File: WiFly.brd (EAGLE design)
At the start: 45.7 x 35.9 mm, 33 parts

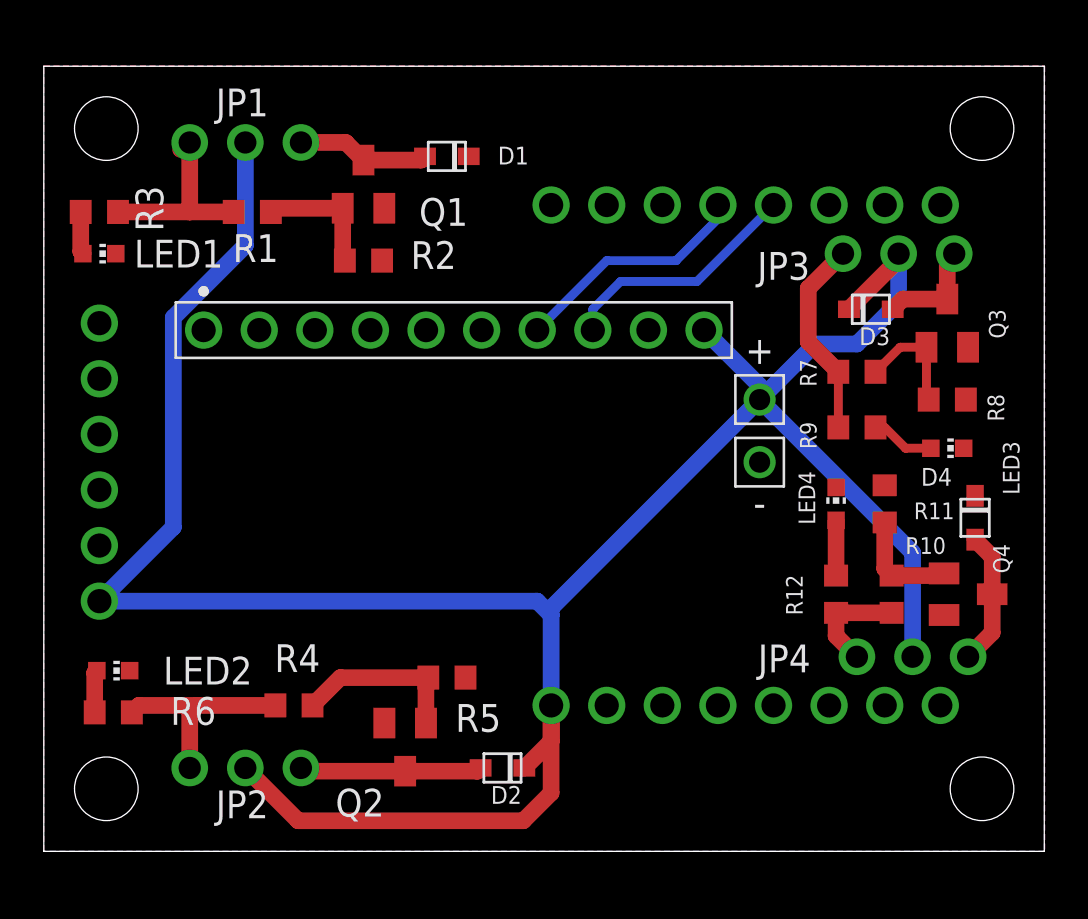
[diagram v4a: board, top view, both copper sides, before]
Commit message: Routed remaining wires and polygon pour, no errors ERC detected
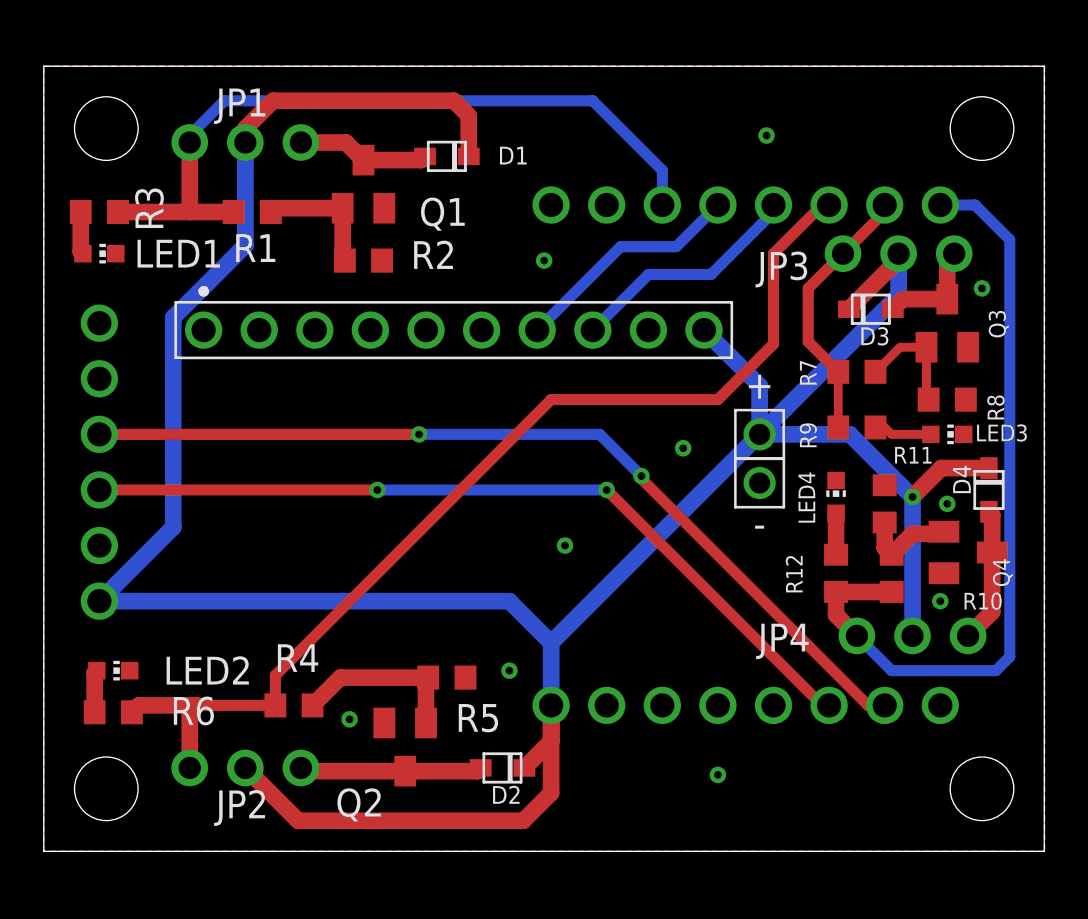
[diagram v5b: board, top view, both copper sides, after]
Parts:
- moved Q4 1.91 mm to (41.6, 11.7)
- moved + 1.59 mm to (32.1, 17.1)
- moved D4 1.42 mm to (42.5, 14.6)
- moved - 0.95 mm to (32.1, 14.9)
- moved R10 0.95 mm to (38.1, 10.8)
- moved R12 0.95 mm to (35.6, 10.8)
- moved JP4 0.95 mm to (39.1, 7.94)
- moved LED3 0.63 mm to (40.6, 17.1)
- moved LED4 0.32 mm to (35.6, 14.3)
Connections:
- removed net TODO1: JP4.1, R10.1, R12.2
- removed net TODO2: JP3.1, R7.1, R9.2
- removed net TODO3: JP2.1, R4.1, R6.2
- removed net TODO4: JP1.1, R1.1, R3.2
- net GPIO12: now also JP1.1, R1.1, R3.2
- net GPIO14: now also JP2.1, R4.1, R6.2
- net GPIO2: now also JP3.1, R7.1, R9.2
- net GPIO4: now also JP4.1, R10.1, R12.2
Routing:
- net GPIO14: track 0.00 -> 47.7 mm
- net TX: track 0.00 -> 41.1 mm, vias 0 -> 2
- net RX: track 0.00 -> 37.4 mm, vias 0 -> 2
- net GPIO4: track 0.00 -> 35.7 mm
- net GPIO12: track 0.00 -> 33.9 mm
- net VCC: track 118.2 -> 136.6 mm, vias 0 -> 1
- net GPIO2: track 0.00 -> 12.2 mm
- net TODO3: track 9.68 -> 0.00 mm
- net TODO2: track 9.16 -> 0.00 mm
- net TODO4: track 9.01 -> 0.00 mm
- net TODO1: track 4.94 -> 0.00 mm
- net N$15: track 2.53 -> 1.89 mm
- net N$14: track 4.99 -> 4.43 mm

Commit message: Widened board a bit to provide clearance for mounting screws. Rev 1 FingersCrossed
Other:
- board size 45.7 x 35.9 mm -> 45.7 x 37.5 mm
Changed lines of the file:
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@@
 <board>
 <plain>
-<wire x1="-0.635" y1="-1.905" x2="45.0725" y2="-1.905" width="0" layer="20"/>
-<wire x1="45.0725" y1="-1.905" x2="45.0725" y2="33.9625" width="0" layer="20"/>
-<wire x1="45.0725" y1="33.9625" x2="-0.635" y2="33.9625" width="0" layer="20"/>
-<wire x1="-0.635" y1="33.9625" x2="-0.635" y2="-1.905" width="0" layer="20"/>
-<hole x="2.2225" y="31.115" drill="2.905759375"/>
-<hole x="42.2275" y="31.115" drill="2.905759375"/>
-<hole x="2.2225" y="0.9525" drill="2.905759375"/>
-<hole x="42.2275" y="0.9525" drill="2.905759375"/>
+<wire x1="-0.635" y1="-2.8575" x2="45.0725" y2="-2.8575" width="0" layer="20"/>
+<wire x1="45.0725" y1="-2.8575" x2="45.0725" y2="34.5975" width="0" layer="20"/>
+<wire x1="45.0725" y1="34.5975" x2="-0.635" y2="34.5975" width="0" layer="20"/>
+<wire x1="-0.635" y1="34.5975" x2="-0.635" y2="-2.8575" width="0" layer="20"/>
+<hole x="2.2225" y="31.75" drill="2.905759375"/>
+<hole x="42.2275" y="31.75" drill="2.905759375"/>
+<hole x="2.2225" y="0" drill="2.905759375"/>
+<hole x="42.2275" y="0" drill="2.905759375"/>
 </plain>
 <attributes>
@@
 <contactref element="-" pad="1"/>
 <polygon width="0.4064" layer="16" isolate="0.254">
-<vertex x="-0.635" y="-1.905"/>
-<vertex x="-0.635" y="33.9725"/>
-<vertex x="45.085" y="33.9725"/>
-<vertex x="45.085" y="-1.905"/>
+<vertex x="-0.635" y="-2.8575"/>
+<vertex x="-0.635" y="34.6075"/>
+<vertex x="45.085" y="34.6075"/>
+<vertex x="45.085" y="-2.8575"/>
 </polygon>
 <polygon width="0.4064" layer="1" isolate="0.254">
-<vertex x="-0.635" y="-1.905"/>
-<vertex x="-0.635" y="33.9725"/>
-<vertex x="45.085" y="33.9725"/>
-<vertex x="45.085" y="-1.905"/>
+<vertex x="-0.635" y="-2.8575"/>
+<vertex x="-0.635" y="34.6075"/>
+<vertex x="45.085" y="34.6075"/>
+<vertex x="45.085" y="-2.8575"/>
 </polygon>
 <contactref element="U$2" pad="12"/>
@@
 <via x="40.64" y="13.97" extent="1-16" drill="0.35"/>
 <via x="42.2275" y="23.8125" extent="1-16" drill="0.35"/>
+<via x="10.4775" y="19.3675" extent="1-16" drill="0.35"/>
+<via x="8.5725" y="12.065" extent="1-16" drill="0.35"/>
+<via x="31.75" y="12.065" extent="1-16" drill="0.35"/>
 </signal>
 <signal name="N$2">
@@
 <contactref element="U$2" pad="14"/>
 <contactref element="U$3" pad="3"/>
-<wire x1="1.905" y1="14.605" x2="14.605" y2="14.605" width="0.508" layer="1"/>
-<via x="14.605" y="14.605" extent="1-16" drill="0.35"/>
-<wire x1="14.605" y1="14.605" x2="25.0825" y2="14.605" width="0.508" layer="16"/>
+<wire x1="1.905" y1="14.605" x2="13.335" y2="14.605" width="0.508" layer="1"/>
+<via x="13.335" y="14.605" extent="1-16" drill="0.35"/>
+<wire x1="13.335" y1="14.605" x2="25.0825" y2="14.605" width="0.508" layer="16"/>
 <via x="25.0825" y="14.605" extent="1-16" drill="0.35"/>
 <wire x1="34.925" y1="4.7625" x2="25.0825" y2="14.605" width="0.508" layer="1"/>
@@
 <contactref element="U$2" pad="15"/>
 <contactref element="U$3" pad="4"/>
-<via x="16.51" y="17.145" extent="1-16" drill="0.35"/>
-<wire x1="16.51" y1="17.145" x2="24.765" y2="17.145" width="0.508" layer="16"/>
+<via x="14.9225" y="17.145" extent="1-16" drill="0.35"/>
+<wire x1="14.9225" y1="17.145" x2="24.765" y2="17.145" width="0.508" layer="16"/>
 <wire x1="24.765" y1="17.145" x2="26.67" y2="15.24" width="0.508" layer="16"/>
 <via x="26.67" y="15.24" extent="1-16" drill="0.35"/>
@@
 <wire x1="26.67" y1="15.24" x2="26.67" y2="15.115425" width="0.508" layer="1"/>
 <wire x1="37.022925" y1="4.7625" x2="37.7825" y2="4.7625" width="0.508" layer="1"/>
-<wire x1="1.905" y1="17.145" x2="16.51" y2="17.145" width="0.508" layer="1"/>
+<wire x1="1.905" y1="17.145" x2="14.9225" y2="17.145" width="0.508" layer="1"/>
 </signal>
 <signal name="GPIO14">

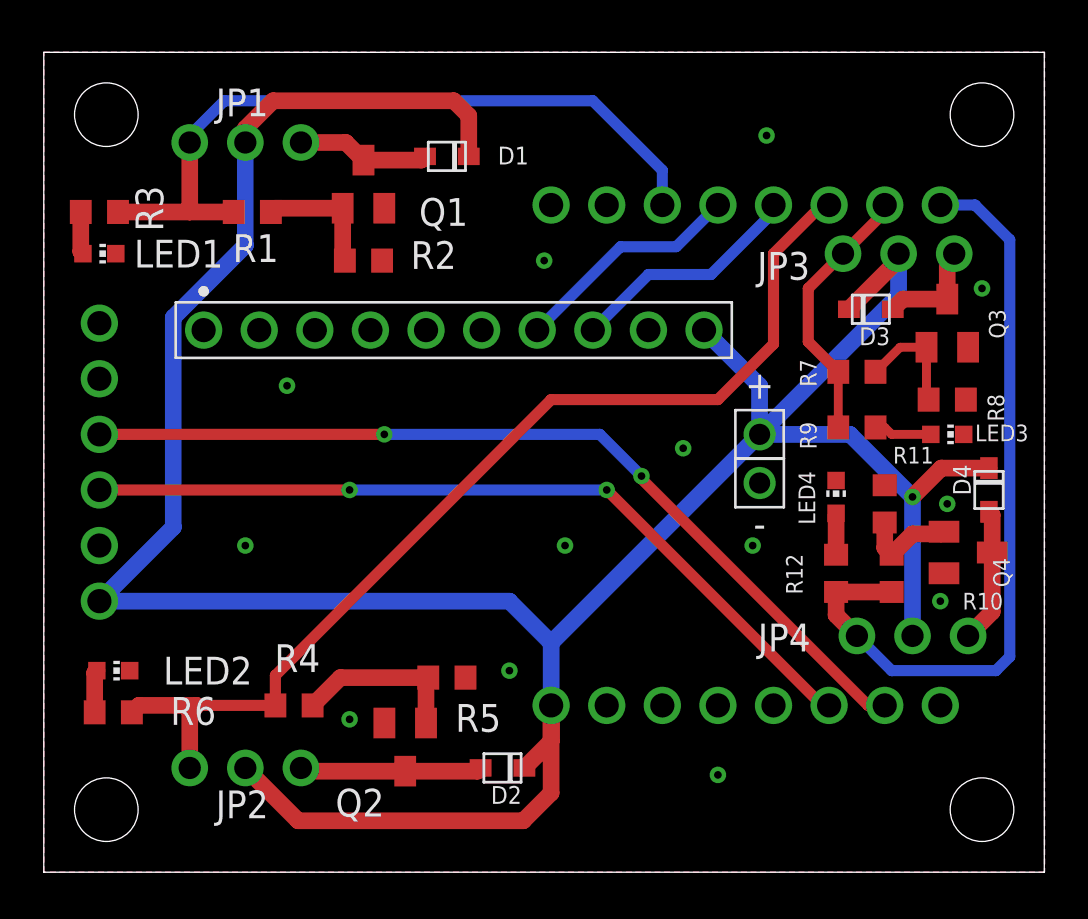
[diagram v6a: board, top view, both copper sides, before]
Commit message: Fix ESP32 layout and slide location down
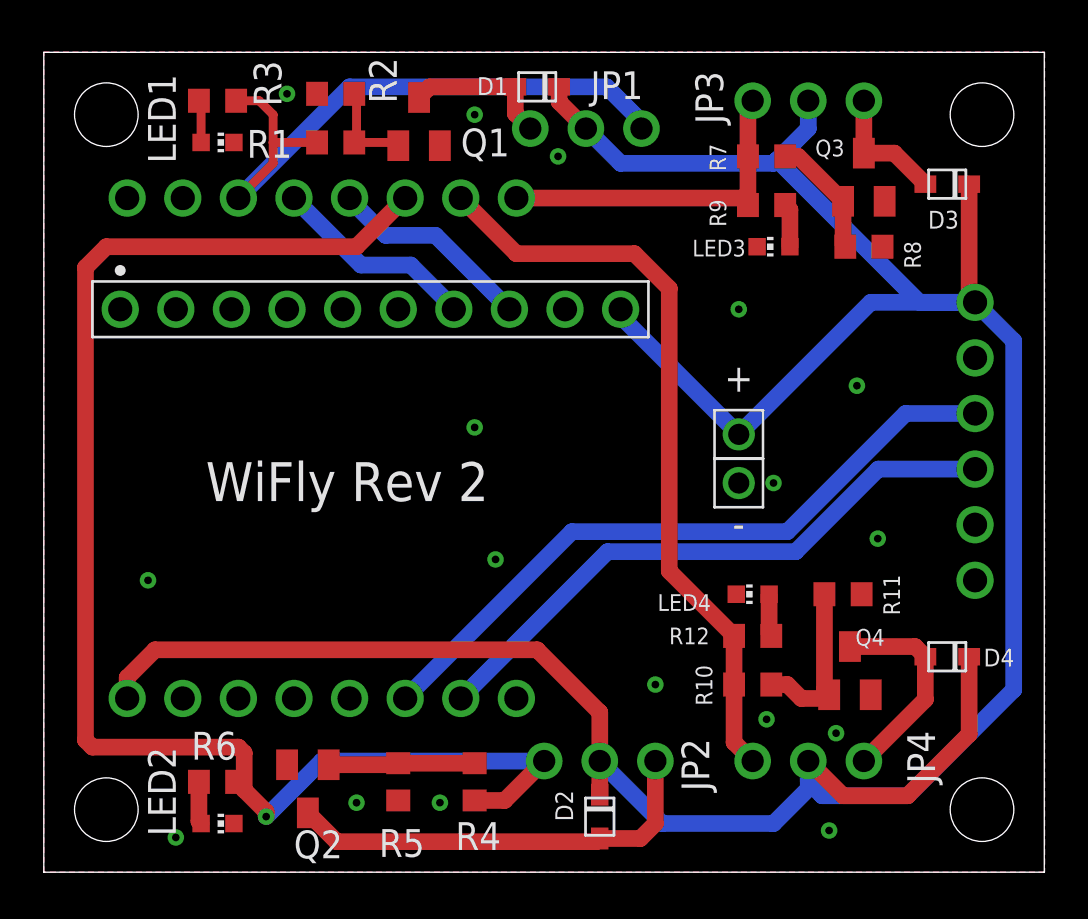
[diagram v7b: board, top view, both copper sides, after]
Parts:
- moved U$3 42.3 mm to (41.9, 23.2), turned to 270 degrees
- moved U$2 19.4 mm to (21.0, 27.9)
- moved JP2 16.2 mm to (24.8, 2.22)
- moved JP1 15.6 mm to (24.1, 31.1), turned to 180 degrees
- moved LED3 11.7 mm to (32.7, 25.7), turned to 90 degrees
- moved R9 11.0 mm to (32.4, 27.6)
- moved R7 10.7 mm to (32.4, 29.8)
- moved R4 8.96 mm to (19.1, 1.27), turned to 90 degrees
- moved LED2 8.45 mm to (7.30, -0.64)
- moved R10 8.13 mm to (31.8, 5.71), turned to 0 degrees
- moved JP3 8.11 mm to (34.3, 32.4)
- moved R8 7.96 mm to (36.8, 25.7)
- moved D4 7.85 mm to (40.6, 6.99), turned to 0 degrees
- moved R2 7.73 mm to (12.7, 32.7), turned to 0 degrees
- moved Q3 7.68 mm to (36.8, 28.9)
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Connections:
- net GPIO2: now also JP4.1, R10.1, R12.2; no longer JP3.1, R7.1, R9.2
- net GPIO4: now also JP3.1, R7.1, R9.2; no longer JP4.1, R10.1, R12.2
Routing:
- net GPIO2: track 12.2 -> 34.4 mm
- net GPIO4: track 35.7 -> 15.6 mm
- net GPIO14: track 47.7 -> 66.5 mm, vias 0 -> 1
- net TX: track 41.1 -> 27.8 mm, vias 2 -> 0
- net N$8: track 8.33 -> 19.6 mm
- net RX: track 37.4 -> 31.4 mm, vias 2 -> 0
- net GPIO12: track 33.9 -> 29.9 mm
- net N$16: track 6.18 -> 9.56 mm
- net N$14: track 4.43 -> 7.66 mm
- net VCC: track 136.6 -> 138.1 mm, vias 1 -> 0
- net N$2: track 5.78 -> 4.34 mm
- net SCL: track 10.8 -> 9.44 mm
- net N$6: track 7.93 -> 6.70 mm
- net SDA: track 10.6 -> 9.44 mm
- net N$12: track 4.89 -> 5.79 mm
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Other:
- board text added: "WiFly Rev 2"

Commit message: Make compatible with lower power battery connection
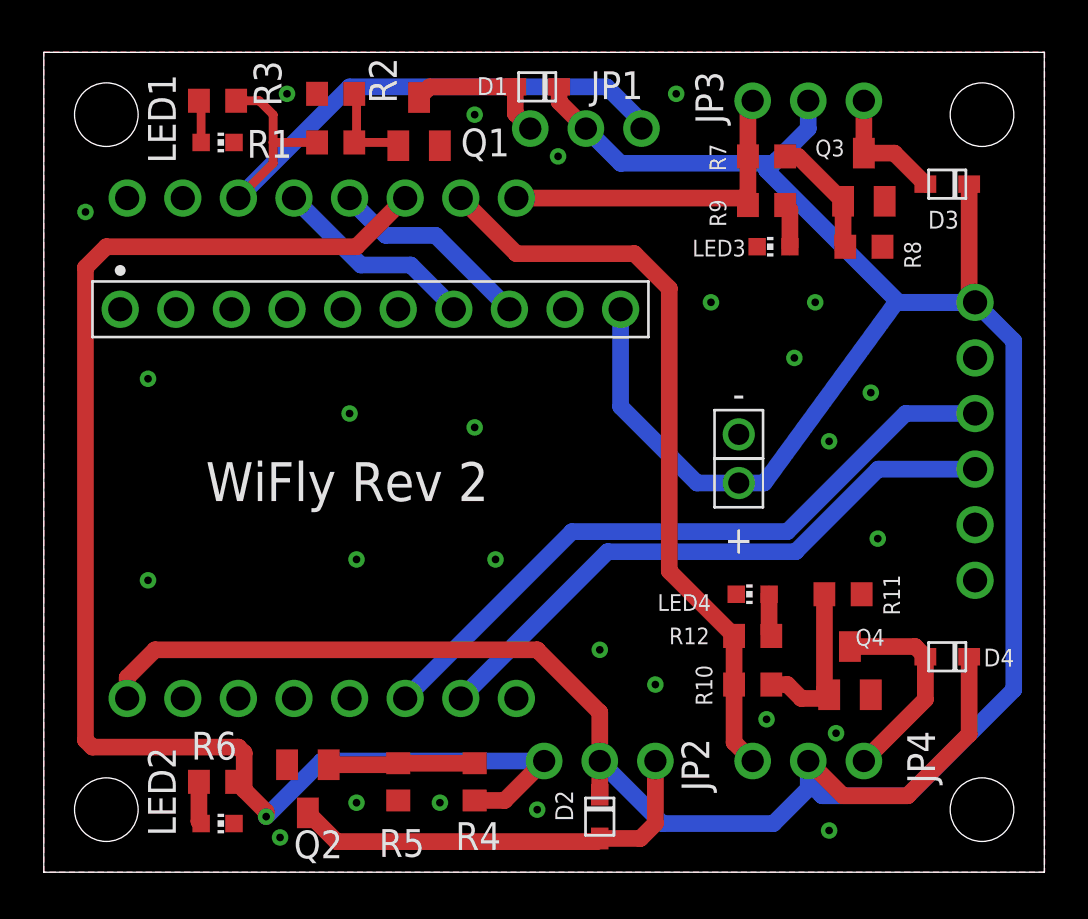
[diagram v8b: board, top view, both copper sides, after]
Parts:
- moved + 2.22 mm to (31.1, 14.9), turned to 270 degrees
- moved - 2.22 mm to (31.1, 17.1), turned to 0 degrees
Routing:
- net VCC: track 138.1 -> 143.8 mm
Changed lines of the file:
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@@
 <attribute name="VALUE" x="32.639" y="9.9695" size="1.27" layer="27" rot="R180"/>
 </element>
-<element name="+" library="WiFlyParts" package="HDRV1W64P0_1X1_193X193X447B" package3d_urn="urn:adsk.eagle:package:26906388/1" value="22AWG22AWG-MALE" x="31.115" y="17.145" smashed="yes" rot="R90">
-<attribute name="NAME" x="31.115" y="20.3644" size="1.27" layer="25" rot="R180" align="bottom-center"/>
+<element name="+" library="WiFlyParts" package="HDRV1W64P0_1X1_193X193X447B" package3d_urn="urn:adsk.eagle:package:26906388/1" value="22AWG22AWG-MALE" x="31.115" y="14.9225" smashed="yes" rot="R270">
+<attribute name="NAME" x="31.115" y="11.7031" size="1.27" layer="25" align="bottom-center"/>
 </element>
-<element name="-" library="WiFlyParts" package="HDRV1W64P0_1X1_193X193X447B" package3d_urn="urn:adsk.eagle:package:26906388/1" value="22AWG22AWG-MALE" x="31.115" y="14.9225" smashed="yes" rot="R180">
-<attribute name="NAME" x="31.115" y="13.6969" size="1.27" layer="25" rot="R180" align="bottom-center"/>
+<element name="-" library="WiFlyParts" package="HDRV1W64P0_1X1_193X193X447B" package3d_urn="urn:adsk.eagle:package:26906388/1" value="22AWG22AWG-MALE" x="31.115" y="17.145" smashed="yes">
+<attribute name="NAME" x="31.115" y="18.3706" size="1.27" layer="25" align="bottom-center"/>
 </element>
 </elements>
@@
 <via x="32.385" y="4.1275" extent="1-16" drill="0.35"/>
 <via x="35.56" y="3.4925" extent="1-16" drill="0.35"/>
-<via x="5.3975" y="-1.27" extent="1-16" drill="0.35"/>
+<via x="10.16" y="-1.27" extent="1-16" drill="0.35"/>
 <via x="10.4775" y="32.7025" extent="1-16" drill="0.35"/>
 <via x="13.6525" y="0.3175" extent="1-16" drill="0.35"/>
@@
 <via x="19.05" y="31.75" extent="1-16" drill="0.35"/>
 <via x="35.2425" y="-0.9525" extent="1-16" drill="0.35"/>
-<via x="36.5125" y="19.3675" extent="1-16" drill="0.35"/>
+<via x="37.1475" y="19.05" extent="1-16" drill="0.35"/>
 <via x="19.05" y="17.4625" extent="1-16" drill="0.35"/>
 <via x="37.465" y="12.3825" extent="1-16" drill="0.35"/>
 <via x="4.1275" y="10.4775" extent="1-16" drill="0.35"/>
 <via x="27.305" y="5.715" extent="1-16" drill="0.35"/>
-<via x="31.115" y="22.86" extent="1-16" drill="0.35"/>
+<via x="29.845" y="23.1775" extent="1-16" drill="0.35"/>
 <via x="22.86" y="29.845" extent="1-16" drill="0.35"/>
 <via x="20.0025" y="11.43" extent="1-16" drill="0.35"/>
-<via x="32.7025" y="14.9225" extent="1-16" drill="0.35"/>
+<via x="35.2425" y="16.8275" extent="1-16" drill="0.35"/>
+<via x="13.335" y="18.0975" extent="1-16" drill="0.35"/>
+<via x="34.6075" y="23.1775" extent="1-16" drill="0.35"/>
+<via x="24.765" y="7.3025" extent="1-16" drill="0.35"/>
+<via x="21.9075" y="0" extent="1-16" drill="0.35"/>
+<via x="4.1275" y="19.685" extent="1-16" drill="0.35"/>
+<via x="28.2575" y="32.7025" extent="1-16" drill="0.35"/>
+<via x="33.655" y="20.6375" extent="1-16" drill="0.35"/>
+<via x="1.27" y="27.305" extent="1-16" drill="0.35"/>
+<via x="13.6525" y="11.43" extent="1-16" drill="0.35"/>
 </signal>
 <signal name="N$2">
@@
 <wire x1="25.7175" y1="29.5275" x2="32.7025" y2="29.5275" width="0.762" layer="16"/>
 <wire x1="32.7025" y1="29.5275" x2="32.86125" y2="29.68625" width="0.762" layer="16"/>
+<wire x1="32.385" y1="29.21" x2="32.7025" y2="29.5275" width="0.762" layer="16"/>
 <wire x1="32.86125" y1="29.68625" x2="34.29" y2="31.115" width="0.762" layer="16"/>
 <wire x1="34.29" y1="31.115" x2="34.29" y2="32.385" width="0.762" layer="16"/>
-<wire x1="41.91" y1="23.1775" x2="39.37" y2="23.1775" width="0.762" layer="16"/>
-<wire x1="39.37" y1="23.1775" x2="32.86125" y2="29.68625" width="0.762" layer="16"/>
+<wire x1="41.91" y1="23.1775" x2="38.4175" y2="23.1775" width="0.762" layer="16"/>
+<wire x1="38.4175" y1="23.1775" x2="32.385" y2="29.21" width="0.762" layer="16"/>
 <wire x1="41.91" y1="23.1775" x2="43.6755" y2="21.412" width="0.762" layer="16"/>
 <wire x1="43.6755" y1="21.412" x2="43.6755" y2="5.47834375" width="0.762" layer="16"/>
@@
 <wire x1="34.29" y1="1.27" x2="34.29" y2="2.2225" width="0.762" layer="16"/>
 <wire x1="38.83215625" y1="0.635" x2="34.925" y2="0.635" width="0.762" layer="16"/>
-<wire x1="31.115" y1="17.145" x2="37.1475" y2="23.1775" width="0.762" layer="16"/>
-<wire x1="37.1475" y1="23.1775" x2="41.91" y2="23.1775" width="0.762" layer="16"/>
-<wire x1="25.7175" y1="22.86" x2="25.7175" y2="22.5425" width="0.762" layer="16"/>
-<wire x1="31.115" y1="17.145" x2="25.7175" y2="22.5425" width="0.762" layer="16"/>
+<wire x1="31.115" y1="14.9225" x2="32.27509375" y2="14.9225" width="0.762" layer="16"/>
+<wire x1="38.307596875" y1="23.1775" x2="32.27509375" y2="14.9225" width="0.762" layer="16"/>
+<wire x1="38.307596875" y1="23.1775" x2="41.91" y2="23.1775" width="0.762" layer="16"/>
+<wire x1="25.7175" y1="22.86" x2="25.7175" y2="18.415" width="0.762" layer="16"/>
+<wire x1="31.115" y1="14.9225" x2="29.21" y2="14.9225" width="0.762" layer="16"/>
+<wire x1="29.21" y1="14.9225" x2="25.7175" y2="18.415" width="0.762" layer="16"/>
 <wire x1="41.64" y1="28.575" x2="41.64" y2="23.4475" width="0.762" layer="1"/>
 <wire x1="41.64" y1="23.4475" x2="41.91" y2="23.1775" width="0.762" layer="1"/>
